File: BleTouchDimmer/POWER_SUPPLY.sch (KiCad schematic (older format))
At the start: 1 part

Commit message: Selected diode bridge.
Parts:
- added D5: Diode_Bridge, EgertKiCad_lib:SOIC-4, symbol Diode_Bridge
- gave numbers to parts that had none: 1
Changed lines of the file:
@@
 http://www.mouser.ee/ProductDetail/Power-Integrations/LNK4002S-TL/?qs=sGAEpiMZZMvzv9EAOJZmO0dg70J8dH5iUaCijAFdjy8%3d
 $Comp
-L LNK4002S U?
+L LNK4002S U5
 U 1 1 58263DA0
 P 4950 3850
-F 0 "U?" H 5000 4500 60  0000 C CNN
+F 0 "U5" H 5000 4500 60  0000 C CNN
 F 1 "LNK4002S" H 5150 4600 60  0000 C CNN
 F 2 "TO_SOT_Packages_SMD:SOT-23-6" H 4950 3850 60  0001 C CNN
@@
 	1    0    0    -1
 $EndComp
+$Comp
+L Diode_Bridge D5
+U 1 1 5826D5CE
+P 2750 3600
+F 0 "D5" H 2500 3900 50  0000 C CNN
+F 1 "Diode_Bridge" H 3100 3250 50  0000 C CNN
+F 2 "EgertKiCad_lib:SOIC-4" H 2750 3600 50  0001 C CNN
+F 3 "http://www.mouser.com/ds/2/149/MB6S-1011197.pdf" H 2750 3600 50  0001 C CNN
+F 4 "http://www.mouser.ee/ProductDetail/Fairchild-Semiconductor/MB6S/?qs=sGAEpiMZZMtQ8nqTKtFS%2fLDhWhDI65nsM5pfIld1Hhg%3d" H 2750 3600 60  0001 C CNN "Ordering"
+	1    2750 3600
+	1    0    0    -1
+$EndComp

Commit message: Added isolation transformer:D
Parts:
- added TR?: TEZ1.5-D-1, TEZ-28x33, symbol TEZ1.5-D-1
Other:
- note added: "http://www.premiermag.com/html/sales/sales.html"
- note added: "http://www.premiermag.com/pdf/PM_Power_Catalog_Abacus_07-09-15.pdf"
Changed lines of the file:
@@
+	1    0    0    -1
+$EndComp
+Text Notes 1850 2600 0    60   ~ 0
+http://www.premiermag.com/pdf/PM_Power_Catalog_Abacus_07-09-15.pdf
+Text Notes 1900 2750 0    60   ~ 0
+http://www.premiermag.com/html/sales/sales.html
+$Comp
+L TEZ1.5-D-1 TR?
+U 1 1 582CA6AB
+P 6450 4450
+F 0 "TR?" H 6450 4700 50  0000 C CNN
+F 1 "TEZ1.5-D-1" H 6450 4200 50  0000 C CNN
+F 2 "TEZ-28x33" H 6450 4100 50  0000 C CIN
+F 3 "http://www.tme.eu/en/Document/0ee0099c912b0b008223c99a7304714f/TEZ-EN.pdf" H 6450 4450 50  0001 C CNN
+F 4 "http://www.tme.eu/en/details/tez1.5_d_6v/pcb-transformers/breve-tufvassons/tez15d2306v/" H 6450 4450 60  0001 C CNN "Ordering"
+	1    6450 4450
 	1    0    0    -1
 $EndComp

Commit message: Updated power supply with LDO LD1117. TODO - Protection (VARISTOR, ??)
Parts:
- removed U5: LNK4002S, TO_SOT_Packages_SMD:SOT-23-6, symbol LNK4002S
- added C5: 1000uF, Capacitors_ThroughHole:C_Radial_D10_L13_P5, symbol CP
- added C6: 10uF, Capacitors_SMD:C_0805, symbol C
- added C8: 22uF, Capacitors_SMD:C_0805, symbol C
- added D6: Led_Small, Resistors_SMD:R_0603_HandSoldering, symbol Led_Small
- added R21: 100R, Resistors_SMD:R_0805, symbol R
- added U5: LD1117S33TR, SOT-223, symbol LD1117S33TR
- gave numbers to parts that had none: 1
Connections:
- net labels added: +3.3V, GND
- wire segments 0 -> 19
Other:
- note removed: "http://electronics.stackexchange.com/questions/101818/surface-mount-transformerless-230v-to-3-3v-on-a-small-board"
- note removed: "http://electronics.stackexchange.com/questions/67295/converting-universal-ac-to-3-3v-dc-0-1a"
- note removed: "http://www.mouser.com/ds/2/328/linkswitch-4_family_datasheet-537370.pdf"
- note removed: "http://www.mouser.ee/ProductDetail/Power-Integrations/LNK4002S-TL/?qs=sGAEpiMZZMvzv9EAOJZmO0dg70J8dH5iUaCijAFdjy8%3d"
- note removed: "http://www.mouser.ee/Semiconductors/Power-Management-ICs/AC-DC-Converters/_/N-64puj/?Ns=Pricing|0"
- note removed: "http://www.premiermag.com/html/sales/sales.html"
- note removed: "http://www.premiermag.com/pdf/PM_Power_Catalog_Abacus_07-09-15.pdf"
- note removed: "http://www.promelec.ru/pdf/lnk501.pdf"
- moved on the sheet: D5, TR3

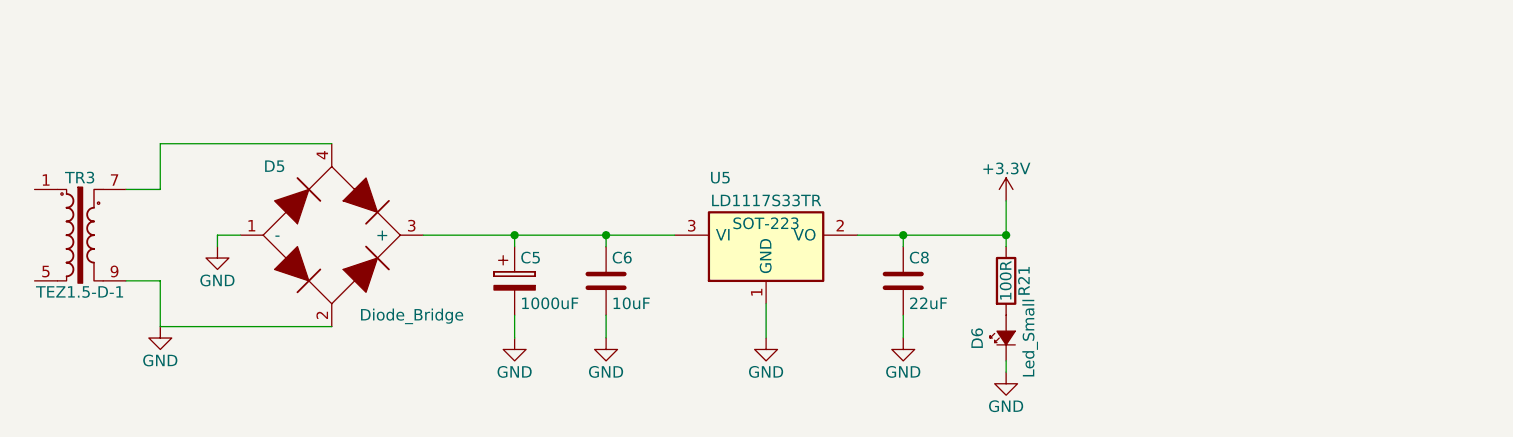
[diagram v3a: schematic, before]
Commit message: Finished power supply and protection circuit, connected all sheets.
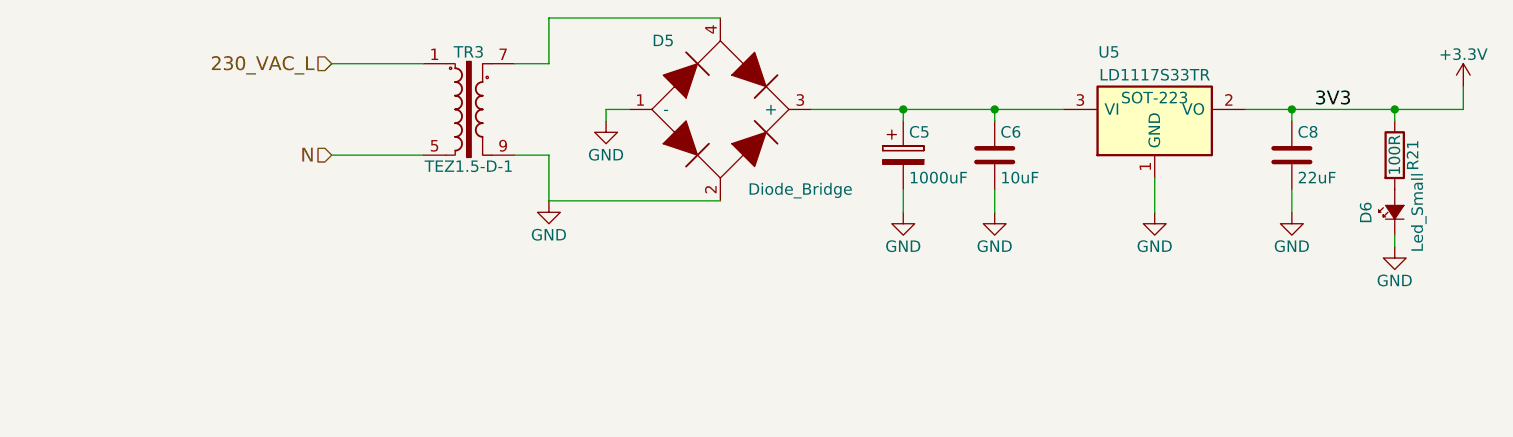
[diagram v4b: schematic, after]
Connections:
- net 230_VAC_L: now reaches TR3.1
- net N: now reaches TR3.5
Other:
- moved on the sheet: C5, C6, C8, D5, D6, R21, TR3, U5

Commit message: Uncommited changes.
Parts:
- C6: footprint Capacitors_SMD:C_0805 -> Capacitors_SMD:C_0603
- C8: footprint Capacitors_SMD:C_0805 -> Capacitors_SMD:C_0603; Spec 16V -> 6V3
- D6: footprint Resistors_SMD:R_0603_HandSoldering -> LEDs:LED_0603
- R21: footprint Resistors_SMD:R_0805 -> Resistors_SMD:R_0603
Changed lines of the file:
@@
 EESchema Schematic File Version 2
+LIBS:BleTouchDimmer-rescue
+LIBS:cypress_touch
+LIBS:azoteq_touch
 LIBS:power
 LIBS:device
@@
 LIBS:Symbols_Microcontroller_Philips-NXP_RevA_06Oct2013
 LIBS:nordicsemi
-LIBS:Egert
 LIBS:Oscillators
 LIBS:74xgxx
@@
 LIBS:microchip_pic16mcu
 LIBS:microchip_pic18mcu
-LIBS:microchip_pic32mcu
 LIBS:motor_drivers
 LIBS:motors
@@
 LIBS:SymbolsSimilarEN60617+oldDIN617-RevE8
 LIBS:BleTouchDimmer-cache
-EELAYER 25 0
+EELAYER 26 0
 EELAYER END
 $Descr A4 11693 8268
@@
 F 0 "C6" H 6225 3400 50  0000 L CNN
 F 1 "10uF" H 6225 3200 50  0000 L CNN
-F 2 "Capacitors_SMD:C_0805" H 6238 3150 50  0001 C CNN
-F 3 "http://www.mouser.ee/ProductDetail/AVX/0805YD106KAT2A/?qs=sGAEpiMZZMsh%252b1woXyUXjwSzqOcIa2sM%252bScaRtZGCJQ%3d" H 6200 3300 50  0001 C CNN
+F 2 "Capacitors_SMD:C_0603" H 6238 3150 50  0001 C CNN
+F 3 "http://www.mouser.ee/ProductDetail/Murata-Electronics/GRM188R61C106KAALJ/?qs=sGAEpiMZZMvsSlwiRhF8qtKev7nvVKumj1MMuNSdQUg4sVWwn51AJA%3d%3d" H 6200 3300 50  0001 C CNN
 F 4 "16V" H 6200 3300 60  0001 C CNN "Spec"
 	1    6200 3300
@@
 F 0 "C8" H 7525 3400 50  0000 L CNN
 F 1 "22uF" H 7525 3200 50  0000 L CNN
-F 2 "Capacitors_SMD:C_0805" H 7538 3150 50  0001 C CNN
-F 3 "http://www.mouser.ee/ProductDetail/Murata-Electronics/GRM21BR60J226ME39L/?qs=sGAEpiMZZMvsSlwiRhF8qqzM%252b6GIxsFQhi2ce6N7jPo%3d" H 7500 3300 50  0001 C CNN
-F 4 "16V" H 7500 3300 60  0001 C CNN "Spec"
+F 2 "Capacitors_SMD:C_0603" H 7538 3150 50  0001 C CNN
+F 3 "http://www.mouser.ee/ProductDetail/AVX/06036D226MAT2A/?qs=sGAEpiMZZMvsSlwiRhF8qkyrPkkEgZV5z45bleISnqh6LLvis9%252b1ig%3d%3d" H 7500 3300 50  0001 C CNN
+F 4 "6V3" H 7500 3300 60  0001 C CNN "Spec"
 	1    7500 3300
 	1    0    0    -1
@@
 F 0 "R21" V 8030 3300 50  0000 C CNN
 F 1 "100R" V 7950 3300 50  0000 C CNN
-F 2 "Resistors_SMD:R_0805" V 7880 3300 50  0001 C CNN
+F 2 "Resistors_SMD:R_0603" V 7880 3300 50  0001 C CNN
 F 3 "" H 7950 3300 50  0000 C CNN
 	1    7950 3300
@@
 F 0 "D6" H 7900 3675 50  0000 L CNN
 F 1 "Led_Small" H 7775 3450 50  0000 L CNN
-F 2 "Resistors_SMD:R_0603_HandSoldering" V 7950 3550 50  0001 C CNN
+F 2 "LEDs:LED_0603" V 7950 3550 50  0001 C CNN
 F 3 "" V 7950 3550 50  0000 C CNN
 	1    7950 3550
